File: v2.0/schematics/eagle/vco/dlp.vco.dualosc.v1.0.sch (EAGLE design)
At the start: 116 parts, among them IC1 NTE912P, IC2 TL074P, IC3 4013N, IC4 TL074P, IC5 TL074P, IC6 NTE912P, IC7 TL072P, J1 PWM, J10 OSC2 OUT, J11 PITCH-2, J12 LIN FM, J2 LIN FM, J3 SQ OUT, J4 EXP FM, J5 PITCH-1, J6 SW OUT, J7 SUB OUT, J8 MIX OUT, Q1 2N3417, Q2 2N3417, Q3 2N3906, Q4 2N3417, Q5 2N3417, Q6 2N3906

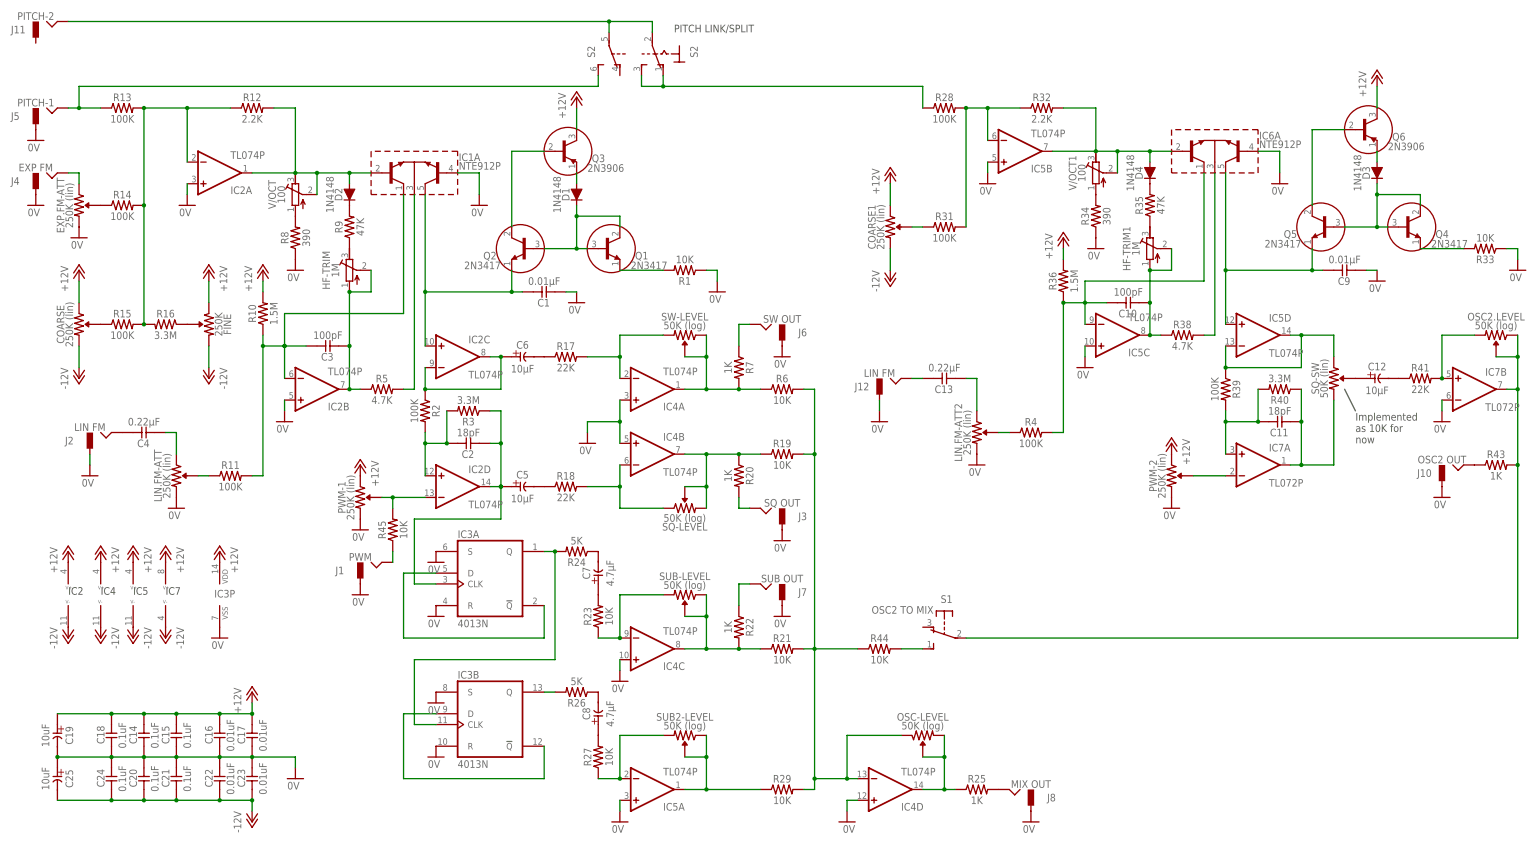
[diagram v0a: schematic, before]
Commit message: Created simplified single version of VCO
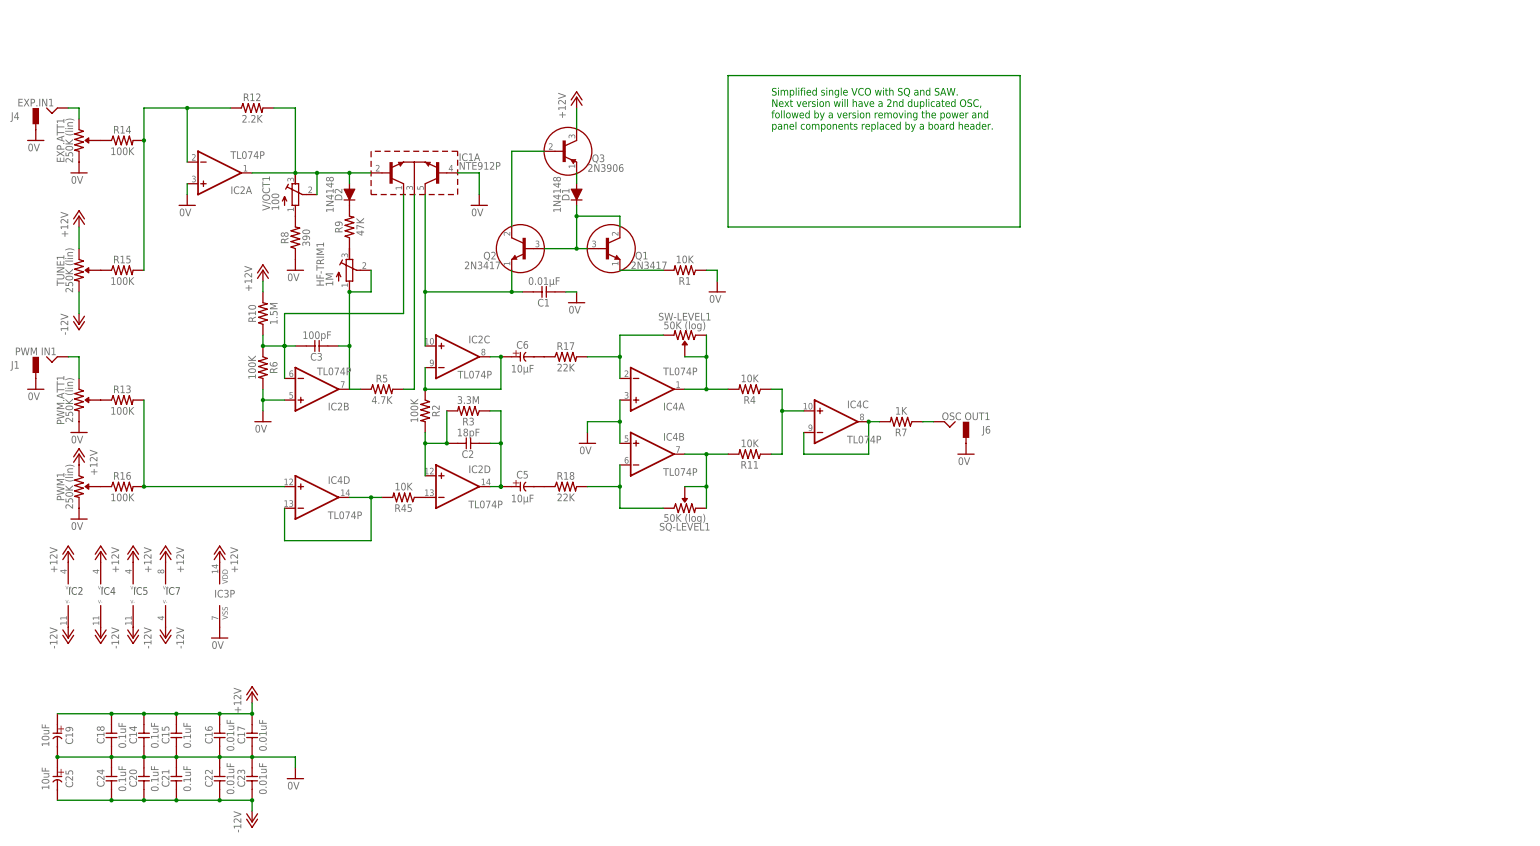
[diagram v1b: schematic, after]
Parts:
- removed C10: 100pF, _common:CC-US025-024X044
- removed C11: 18pF, _common:CC-US025-024X044
- removed C12: 10μF, _common:CE-USE2-5
- removed C13, C4: 0.22μF, _common:CC-US025-024X044
- removed C7, C8: 4.7μF, _common:CE-USE2-5
- removed C9: 0.01μF, _common:CC-US025-024X044
- removed COARSE, COARSE1, EXP.FM-ATT, LIN.FM-ATT, LIN.FM-ATT2, PWM-1, PWM-2: 250K (lin), _common:R-VAR
- removed D3, D4: 1N4148, _common:1N4148
- removed FINE: 250K, _common:R-VAR
- removed HF-TRIM: 1M, _common:R-TRIMM3304W
- removed IC6: NTE912P, _common:NTE912P
- removed J10: OSC2 OUT, _common:JACK-M
- removed J11: PITCH-2, _common:JACK-M
- removed J12, J2: LIN FM, _common:JACK-M
- removed J3: SQ OUT, _common:JACK-M
- removed J5: PITCH-1, _common:JACK-M
- removed J7: SUB OUT, _common:JACK-M
- removed J8: MIX OUT, _common:JACK-M
- removed OSC-LEVEL, OSC2.LEVEL, SUB-LEVEL, SUB2-LEVEL: 50K (log), _common:R-VAR
- removed Q4, Q5: 2N3417, _common:2N3417
- removed Q6: 2N3906, _common:2N3906
- removed R19, R21, R23, R27, R29, R33, R44: 10K, _common:R0309/10
- removed R20, R22, R25, R43: 1K, _common:R0309/10
- removed R24, R26: 5K, _common:R0309/10
- removed R28, R31, R39: 100K, _common:R0309/10
- removed R32: 2.2K, _common:R0309/10
- removed R34: 390, _common:R0309/10
- removed R35: 47K, _common:R0309/10
- removed R36: 1.5M, _common:R0309/10
- removed R38: 4.7K, _common:R0309/10
- removed R40: 3.3M, _common:R0309/10
- removed R41: 22K, _common:R0309/10
- removed S1: OSC2 TO MIX, switch-misc:9077-1
- removed S2: (no value), switch:320-938
- removed SQ-SW: 50K (lin), _common:R-VAR
- removed V/OCT: 100, _common:R-TRIMM3304W
- added EXP.ATT1, PWM.ATT1, PWM1, TUNE1: 250K (lin), _common:R-VAR
- HF-TRIM1, V/OCT1: device _common:R-TRIMM3304W -> rcl:R-TRIMM3296Y
- J1: value PWM -> PWM IN1
- J4: value EXP FM -> EXP.IN1
- J6: value SW OUT -> OSC OUT1
- R11, R4: value 100K -> 10K
- R16: value 3.3M -> 100K
- R6: value 10K -> 100K
- renumbered SQ-LEVEL to SQ-LEVEL1, SW-LEVEL to SW-LEVEL1
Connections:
- removed net N$11: C3.2, HF-TRIM.E, HF-TRIM.S, IC2B.OUT, R5.1
- removed net N$21 (its old number): IC3A.Q, IC3B.CLK, R24.2
- removed net N$33: C7.+, R23.2
- removed net N$36: C7.-, R24.1
- removed net N$39: J7.HOT, R22.1
- removed net N$40: IC4C.-IN, R23.1, SUB-LEVEL.2
- removed net N$41: IC4C.OUT, R21.1, R22.2, SUB-LEVEL.1, SUB-LEVEL.P$1
- removed net N$42: C8.-, R26.1
- removed net N$43: IC3B.Q, R26.2
- removed net N$44: J8.HOT, R25.2
- removed net N$45: C12.-, R41.1
- removed net N$46: IC7A.-IN, PWM-2.P$1
- removed net N$47: IC3B.!Q, IC3B.D
- removed net N$48: C8.+, R27.2
- removed net N$49: IC5A.-IN, R27.1, SUB2-LEVEL.2
- removed net N$50: IC5A.OUT, R29.1, SUB2-LEVEL.1, SUB2-LEVEL.P$1
- removed net N$51: C13.1, J12.HOT
- removed net N$52: COARSE1.P$1, R31.1
- removed net N$54: IC5B.-IN, R28.2, R31.2, R32.1
- removed net N$55: IC4D.OUT, OSC-LEVEL.2, OSC-LEVEL.P$1, R25.1
- removed net N$56: C9.1, IC5D.+IN, Q5.E
- removed net N$57: D3.A, Q6.E
- removed net N$58: Q4.E, R33.2
- removed net N$59: D3.C, Q4.B, Q4.C, Q5.B
- removed net N$60: Q5.C, Q6.B
- removed net N$61: C10.2, HF-TRIM1.E, HF-TRIM1.S, IC5C.OUT, R38.1
- removed net N$62: IC6A.E, R38.2
- removed net N$63: D4.C, R35.2
- removed net N$64: C10.1, IC5C.-IN, R36.1, R4.2
- removed net N$65: D4.A, IC5B.OUT, IC6A.B1, R32.2, V/OCT1.A, V/OCT1.S
- removed net N$66: R34.2, V/OCT1.E
- removed net N$67: HF-TRIM1.A, R35.1
- removed net N$68: IC5D.-IN, IC5D.OUT, R39.1, SQ-SW.1
- removed net N$69: C11.1, IC7A.+IN, R39.2, R40.2
- removed net N$70: C11.2, IC7A.OUT, R40.1, SQ-SW.2
- removed net N$72: C12.+, SQ-SW.P$1
- removed net N$73: IC7B.+IN, OSC2.LEVEL.2, R41.2
- removed net N$74: IC7B.OUT, OSC2.LEVEL.1, OSC2.LEVEL.P$1, R43.2, S1.P
- removed net N$75: J10.HOT, R43.1
- removed net N$76: R44.2, S1.S
- removed net N$77: IC4D.-IN, OSC-LEVEL.1, R19.2, R21.2, R29.2, R44.1, R6.2
- removed net N$78: J5.HOT, R13.1, S2B.S
- removed net N$79: R28.1, S21.O, S21.S
- removed net N$80: LIN.FM-ATT2.P$1, R4.1
- removed net N$81: C13.2, LIN.FM-ATT2.1
- net +12V: now also PWM1.1, TUNE1.1; no longer COARSE.1, COARSE1.1, FINE.1, PWM-1.1, PWM-2.1, Q6.C, R36.2
- net -12V: now also TUNE1.2; no longer COARSE.2, COARSE1.2, FINE.2
- net 0V: now also EXP.ATT1.2, PWM.ATT1.2, PWM1.2, R6.2; no longer C9.2, EXP.FM-ATT.2, IC3A.R, IC3A.S, IC3B.R, IC3B.S, IC4C.+IN, IC4D.+IN, IC5A.+IN, IC5B.+IN, IC5C.+IN, IC6A.B3, IC7B.-IN, J10.GND, J12.GND, J2.GND, J3.GND, J5.GND, J7.GND, J8.GND, LIN.FM-ATT.2, LIN.FM-ATT2.2, PWM-1.2, PWM-2.2, R33.1, R34.1
- net N$10: now also PWM.ATT1.P$1, R13.1; no longer IC2D.-IN, PWM-1.P$1, R45.2
- net N$14: now also V/OCT1.A; no longer V/OCT.E
- net N$15: now also R6.1; no longer R11.2
- net N$16: now also V/OCT1.E, V/OCT1.S; no longer V/OCT.A, V/OCT.S
- net N$17: now also HF-TRIM1.E; no longer HF-TRIM.A
- net N$18: now also IC4C.+IN, R4.1; no longer LIN.FM-ATT.P$1
- net N$19: now also PWM1.P$1, R16.1; no longer C4.2, LIN.FM-ATT.1
- net N$20: now also IC4C.-IN, IC4C.OUT, R7.2; no longer C4.1, J2.HOT
- net N$23: now also EXP.ATT1.P$1; no longer EXP.FM-ATT.P$1
- net N$24: now also TUNE1.P$1; no longer COARSE.P$1
- net N$25: now also J1.HOT, PWM.ATT1.1; no longer FINE.P$1, R16.1
- net N$26: now also EXP.ATT1.1; no longer EXP.FM-ATT.1
- net N$27: now also IC4D.-IN, IC4D.OUT, R45.2; no longer J11.HOT, S21.P, S2B.P
- net N$28: no longer R13.2, R16.2
- net N$31: now also R4.2; no longer R6.1, R7.2
- net N$32: now also R11.2; no longer R19.1, R20.1
- net N$35: now also IC4D.+IN, R13.2, R16.2; no longer IC3A.!Q, IC3A.D
- net N$37: now also C3.2, HF-TRIM1.A, HF-TRIM1.S, IC2B.OUT, R5.1; no longer J3.HOT, R20.2
- net N$8: now also IC2D.-IN; no longer J1.HOT
- net N$9: no longer IC3A.CLK
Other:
- note added: "Simplified single VCO with SQ and SAW. Next version will have a 2nd duplicated OSC, followed by a version removing the power and panel components replaced by a board header."
- note removed: "Implemented as 10K for now"
- note removed: "PITCH LINK/SPLIT"
- moved on the sheet: C3, HF-TRIM1, IC4C, IC4D, J1, J4, J6, R11, R13, R14, R15, R16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

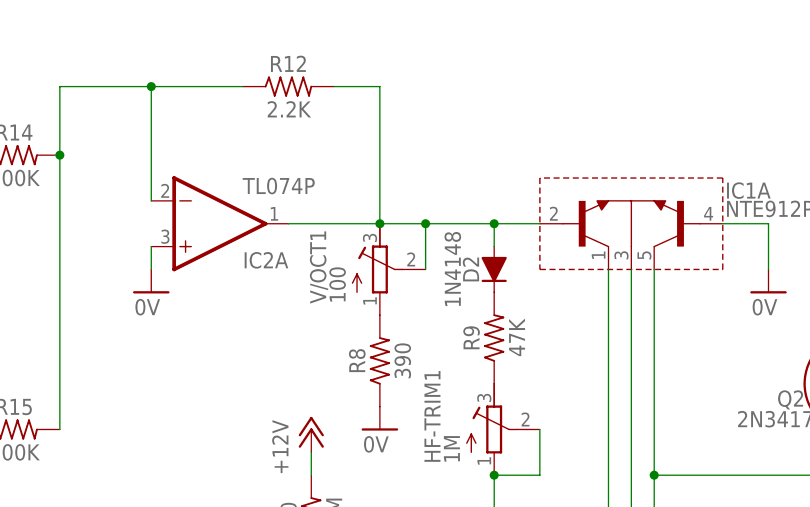
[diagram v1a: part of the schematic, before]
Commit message: Corrected errors on VCO across all versions (board needs to be regenerated)
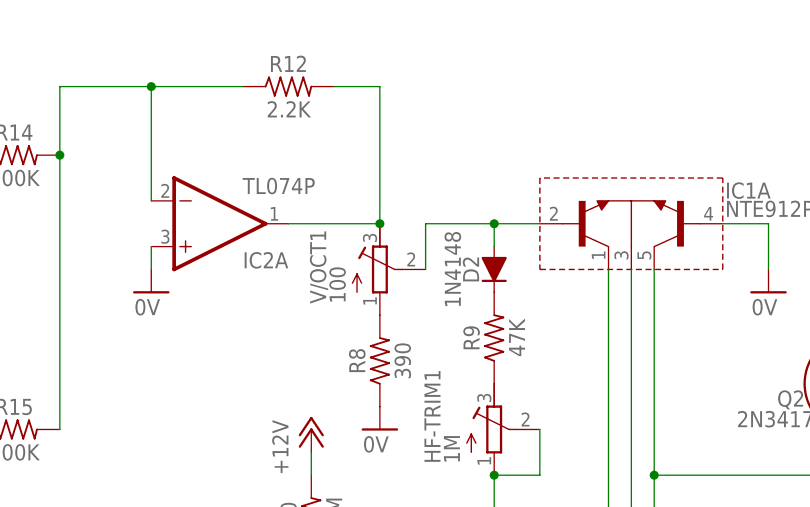
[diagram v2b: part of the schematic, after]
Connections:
- new net N$11: D2.A, IC1A.B1, V/OCT1.S
- net N$16: no longer D2.A, IC1A.B1, V/OCT1.S
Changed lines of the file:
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@@
 <grid distance="0.1" unitdist="inch" unit="inch" style="lines" multiple="1" display="no" altdistance="0.01" altunitdist="inch" altunit="inch"/>
 <layers>
-<layer number="1" name="Top" color="4" fill="1" visible="yes" active="no"/>
-<layer number="16" name="Bottom" color="1" fill="1" visible="yes" active="no"/>
-<layer number="17" name="Pads" color="2" fill="1" visible="yes" active="no"/>
-<layer number="18" name="Vias" color="2" fill="1" visible="yes" active="no"/>
-<layer number="19" name="Unrouted" color="6" fill="1" visible="yes" active="no"/>
-<layer number="20" name="Dimension" color="15" fill="1" visible="yes" active="no"/>
-<layer number="21" name="tPlace" color="7" fill="1" visible="yes" active="no"/>
-<layer number="22" name="bPlace" color="7" fill="1" visible="yes" active="no"/>
-<layer number="23" name="tOrigins" color="15" fill="1" visible="yes" active="no"/>
-<layer number="24" name="bOrigins" color="15" fill="1" visible="yes" active="no"/>
-<layer number="25" name="tNames" color="7" fill="1" visible="yes" active="no"/>
-<layer number="26" name="bNames" color="7" fill="1" visible="yes" active="no"/>
-<layer number="27" name="tValues" color="7" fill="1" visible="yes" active="no"/>
-<layer number="28" name="bValues" color="7" fill="1" visible="yes" active="no"/>
+<layer number="1" name="Top" color="4" fill="1" visible="no" active="no"/>
+<layer number="16" name="Bottom" color="1" fill="1" visible="no" active="no"/>
+<layer number="17" name="Pads" color="2" fill="1" visible="no" active="no"/>
+<layer number="18" name="Vias" color="2" fill="1" visible="no" active="no"/>
+<layer number="19" name="Unrouted" color="6" fill="1" visible="no" active="no"/>
+<layer number="20" name="Dimension" color="15" fill="1" visible="no" active="no"/>
+<layer number="21" name="tPlace" color="7" fill="1" visible="no" active="no"/>
+<layer number="22" name="bPlace" color="7" fill="1" visible="no" active="no"/>
+<layer number="23" name="tOrigins" color="15" fill="1" visible="no" active="no"/>
+<layer number="24" name="bOrigins" color="15" fill="1" visible="no" active="no"/>
+<layer number="25" name="tNames" color="7" fill="1" visible="no" active="no"/>
+<layer number="26" name="bNames" color="7" fill="1" visible="no" active="no"/>
+<layer number="27" name="tValues" color="7" fill="1" visible="no" active="no"/>
+<layer number="28" name="bValues" color="7" fill="1" visible="no" active="no"/>
 <layer number="29" name="tStop" color="7" fill="3" visible="no" active="no"/>
 <layer number="30" name="bStop" color="7" fill="6" visible="no" active="no"/>
@@
 <layer number="35" name="tGlue" color="7" fill="4" visible="no" active="no"/>
 <layer number="36" name="bGlue" color="7" fill="5" visible="no" active="no"/>
-<layer number="37" name="tTest" color="7" fill="1" visible="yes" active="no"/>
-<layer number="38" name="bTest" color="7" fill="1" visible="yes" active="no"/>
+<layer number="37" name="tTest" color="7" fill="1" visible="no" active="no"/>
+<layer number="38" name="bTest" color="7" fill="1" visible="no" active="no"/>
 <layer number="39" name="tKeepout" color="4" fill="11" visible="no" active="no"/>
 <layer number="40" name="bKeepout" color="1" fill="11" visible="no" active="no"/>
@@
 <layer number="44" name="Drills" color="7" fill="1" visible="no" active="no"/>
 <layer number="45" name="Holes" color="7" fill="1" visible="no" active="no"/>
-<layer number="46" name="Milling" color="3" fill="1" visible="yes" active="no"/>
-<layer number="47" name="Measures" color="7" fill="1" visible="yes" active="no"/>
-<layer number="48" name="Document" color="7" fill="1" visible="yes" active="no"/>
-<layer number="49" name="Reference" color="7" fill="1" visible="yes" active="no"/>
-<layer number="50" name="dxf" color="7" fill="1" visible="yes" active="no"/>
-<layer number="51" name="tDocu" color="7" fill="1" visible="yes" active="no"/>
-<layer number="52" name="bDocu" color="7" fill="1" visible="yes" active="no"/>
+<layer number="46" name="Milling" color="3" fill="1" visible="no" active="no"/>
+<layer number="47" name="Measures" color="7" fill="1" visible="no" active="no"/>
+<layer number="48" name="Document" color="7" fill="1" visible="no" active="no"/>
+<layer number="49" name="Reference" color="7" fill="1" visible="no" active="no"/>
+<layer number="50" name="dxf" color="7" fill="1" visible="no" active="no"/>
+<layer number="51" name="tDocu" color="7" fill="1" visible="no" active="no"/>
+<layer number="52" name="bDocu" color="7" fill="1" visible="no" active="no"/>
 <layer number="91" name="Nets" color="2" fill="1" visible="yes" active="yes"/>
 <layer number="92" name="Busses" color="1" fill="1" visible="yes" active="yes"/>
@@
 <pinref part="IC2" gate="A" pin="OUT"/>
 <wire x1="-17.78" y1="68.58" x2="-7.62" y2="68.58" width="0.1524" layer="91"/>
-<pinref part="D2" gate="G$1" pin="A"/>
-<pinref part="IC1" gate="A" pin="B1"/>
-<wire x1="10.16" y1="68.58" x2="5.08" y2="68.58" width="0.1524" layer="91"/>
-<wire x1="5.08" y1="68.58" x2="5.08" y2="66.04" width="0.1524" layer="91"/>
-<junction x="5.08" y="68.58"/>
-<wire x1="-2.54" y1="68.58" x2="5.08" y2="68.58" width="0.1524" layer="91"/>
-<wire x1="-2.54" y1="63.5" x2="-2.54" y2="68.58" width="0.1524" layer="91"/>
-<pinref part="V/OCT1" gate="G$1" pin="S"/>
-<wire x1="-7.62" y1="68.58" x2="-2.54" y2="68.58" width="0.1524" layer="91"/>
 <junction x="-7.62" y="68.58"/>
-<junction x="-2.54" y="68.58"/>
 </segment>
 </net>
@@
 </segment>
 </net>
+<net name="N$11" class="0">
+<segment>
+<pinref part="D2" gate="G$1" pin="A"/>
+<pinref part="IC1" gate="A" pin="B1"/>
+<wire x1="10.16" y1="68.58" x2="5.08" y2="68.58" width="0.1524" layer="91"/>
+<wire x1="5.08" y1="68.58" x2="5.08" y2="66.04" width="0.1524" layer="91"/>
+<junction x="5.08" y="68.58"/>
+<wire x1="-2.54" y1="68.58" x2="5.08" y2="68.58" width="0.1524" layer="91"/>
+<wire x1="-2.54" y1="63.5" x2="-2.54" y2="68.58" width="0.1524" layer="91"/>
+<pinref part="V/OCT1" gate="G$1" pin="S"/>
+</segment>
+</net>
